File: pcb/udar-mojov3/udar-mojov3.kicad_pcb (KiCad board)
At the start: 2 copper layers, 20 parts, among them J1 Conn_02x03_Odd_Even, M1 Motor_Servo_AirTronics, M2 Motor_Servo_AirTronics, Q1 Q_PNP_BCE, Q2 Q_PNP_BCE, SW1 SW_Push, U1 HC-SR04, U2 ZG-Mxx, U3 Mojov3

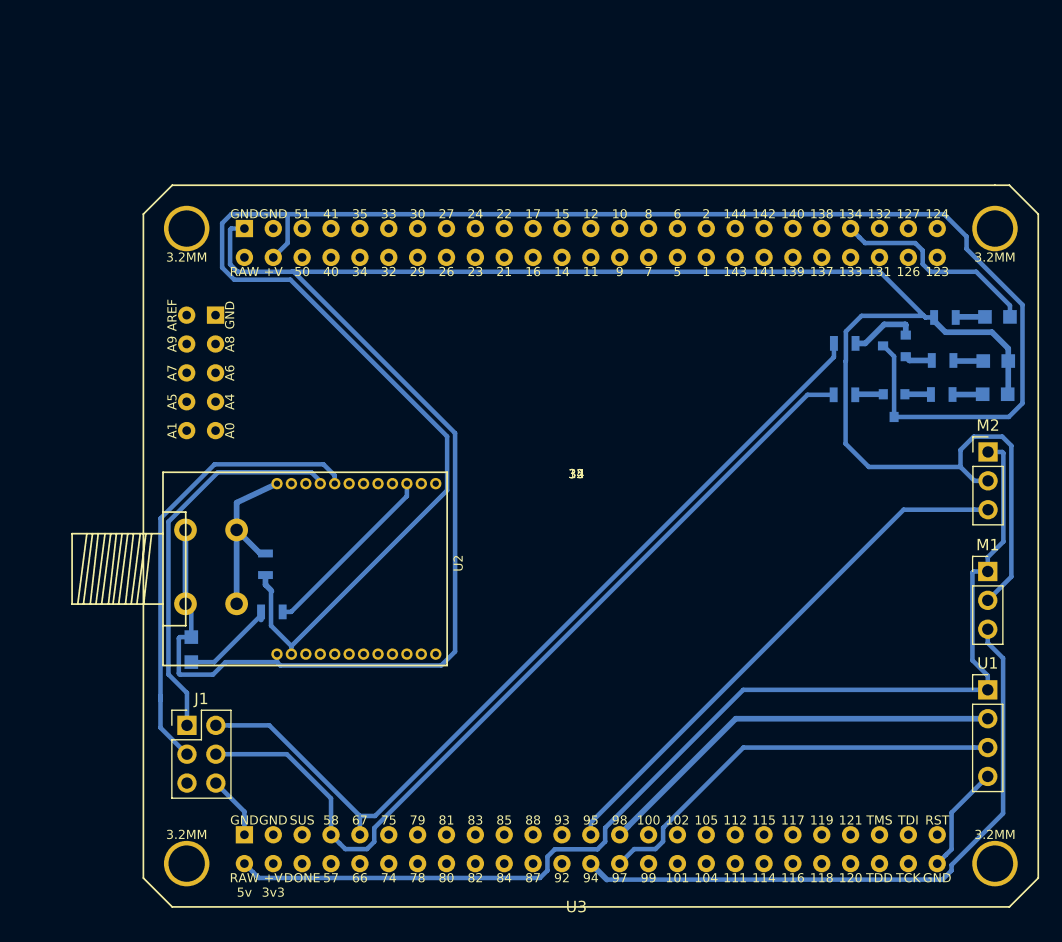
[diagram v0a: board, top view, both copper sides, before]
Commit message: Update
1. Restruct the PCB
2. Change 1602 to OLED(12864)
3. Finish PCB
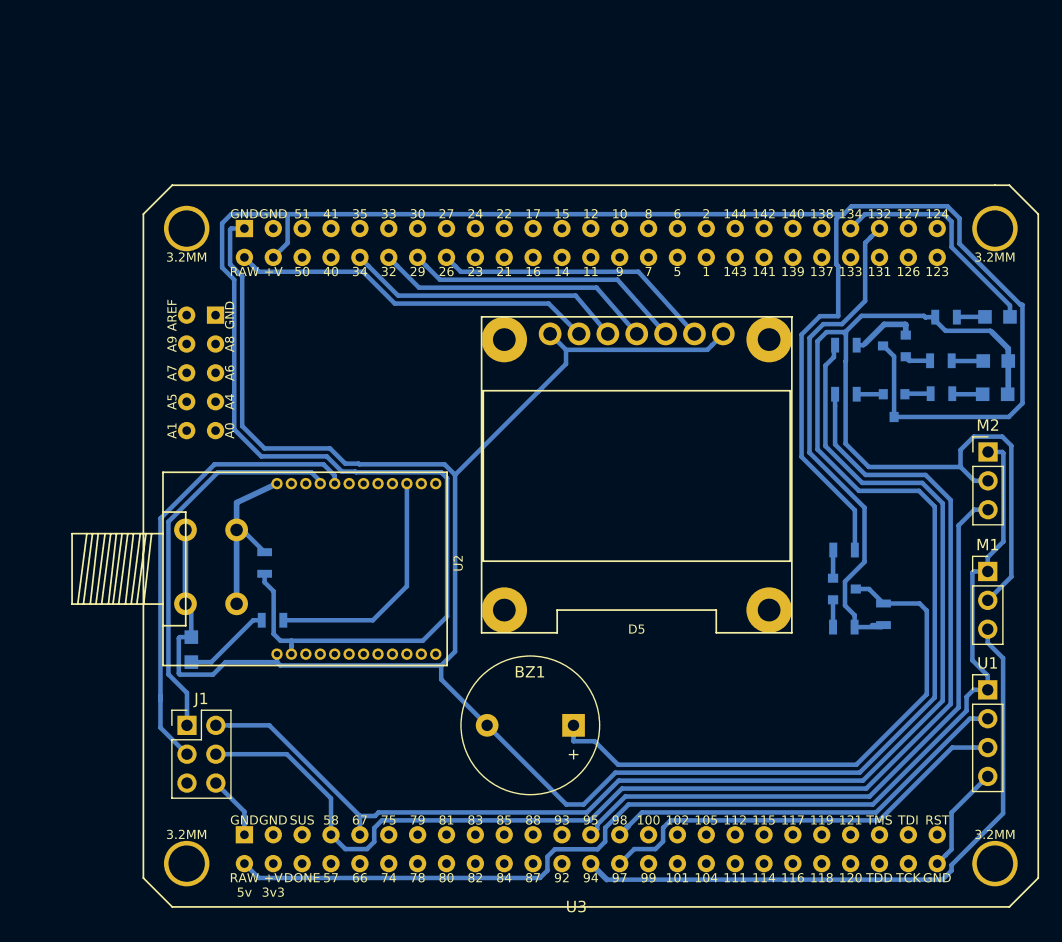
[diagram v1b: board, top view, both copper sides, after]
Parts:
- removed R11: R, Resistors_SMD:R_0805
- added BZ1: Buzzer, Buzzers_Beepers:Buzzer_12x9.5RM7.6, F.Cu at (148.4, 128.6)
- added D5: OLED, OLED:OLED_096_12864_SSD1306, F.Cu at (153.9, 94.2)
- added Q3: Q_NPN_BCE, TO_SOT_Packages_SMD:SOT-23, B.Cu at (172.2, 116.6)
- added R1: R, Resistors_SMD:R_0805, B.Cu at (121.2, 114.3)
- added R2: R, Resistors_SMD:R_0805, B.Cu at (121.9, 119.4)
- added R3: R, Resistors_SMD:R_0805, B.Cu at (172.3, 95.2)
- added R4: R, Resistors_SMD:R_0805, B.Cu at (180.7, 96.5)
- moved R6 62.0 mm to (180.7, 99.4)
- moved R5 53.2 mm to (172.3, 99.5), turned to 180 degrees
- moved R8 25.0 mm to (172.1, 120.0), turned to 180 degrees
- moved R9 19.6 mm to (175.6, 118.9), turned to 90 degrees
- moved R7 18.2 mm to (172.2, 113.2)
- moved R10 6.82 mm to (181.1, 92.7), turned to 180 degrees
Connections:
- net /UDAR-1602a.sch/D0 renamed Net-(U3-Pad33)
- net /UDAR-1602a.sch/D2 renamed Net-(U3-Pad30)
- net /UDAR-1602a.sch/D4 renamed Net-(U3-Pad27)
- net /UDAR-1602a.sch/D6 renamed Net-(U3-Pad24)
- net /UDAR-1602a.sch/D7 renamed Net-(U3-Pad23)
- net /UDAR-1602a.sch/R/W renamed Net-(U3-Pad35)
- net /UDAR-1602a.sch/RS renamed Net-(U3-Pad40)
- R10 pad 1: Net-(Q2-Pad2) -> Net-(D4-Pad1)
- R10 pad 2: Net-(D3-Pad2) -> GND
- R5 pad 1: +3V3 -> Net-(Q2-Pad1)
- R5 pad 2: Net-(R5-Pad2) -> /UART/UART_RX
- R6 pad 1: Net-(D1-Pad2) -> Net-(Q2-Pad2)
- R6 pad 2: Net-(R6-Pad2) -> Net-(D3-Pad2)
- R7 pad 1: Net-(Q1-Pad1) -> +3V3
- R7 pad 2: /UART/UART_TX -> Net-(Q3-Pad2)
- R8 pad 1: Net-(Q1-Pad2) -> Net-(R8-Pad1)
- R8 pad 2: Net-(D2-Pad2) -> Net-(Q3-Pad1)
- R9 pad 1: Net-(Q2-Pad1) -> Net-(R8-Pad1)
- R9 pad 2: /UART/UART_RX -> Net-(BZ1-Pad1)
- SW1 pad 1: Net-(R5-Pad2) -> Net-(R1-Pad2)
- U2 pad B1: Net-(R5-Pad2) -> Net-(R1-Pad2)
- U2 pad B10: Net-(R6-Pad2) -> Net-(R2-Pad2)
- U3 pad 132: Net-(U3-Pad132) -> Net-(R8-Pad1)
- U3 pad 26: /UDAR-1602a.sch/D5 -> /0.96 OLED/DC
- U3 pad 29: /UDAR-1602a.sch/D3 -> /0.96 OLED/RST
- U3 pad 32: /UDAR-1602a.sch/D1 -> /0.96 OLED/DATA
- U3 pad 34: /UDAR-1602a.sch/E -> /0.96 OLED/CLK
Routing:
- net GND: track 227.4 -> 302.3 mm
- net Net-(BZ1-Pad1): track 0.00 -> 50.3 mm
- net +3V3: track 168.2 -> 216.1 mm
- net Net-(R8-Pad1): track 0.00 -> 45.3 mm
- net /UART/UART_TX: track 77.3 -> 112.1 mm
- net /UART/UART_RX: track 77.3 -> 110.6 mm
- net +5V: track 98.8 -> 131.8 mm
- net /0.96 OLED/CLK: track 0.00 -> 24.8 mm
- net /0.96 OLED/DATA: track 0.00 -> 24.8 mm
- net /0.96 OLED/RST: track 0.00 -> 24.8 mm
- net /0.96 OLED/DC: track 0.00 -> 24.8 mm
- net Net-(R2-Pad2): track 0.00 -> 21.7 mm
- net Net-(R1-Pad2): track 0.00 -> 16.6 mm
- net Net-(R6-Pad2): track 16.3 -> 0.00 mm
- net Net-(R5-Pad2): track 16.2 -> 0.00 mm
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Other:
- net class self: clearance 0.3 -> 0.2
- net class self-m added: clearance 0.2, trace_width 0.4, via_dia 0.6, via_drill 0.4

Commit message: Update for 0.1-alpha1
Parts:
- added U4: AP1117-50, TO_SOT_Packages_SMD:SOT-223-3_TabPin2, B.Cu at (127.4, 96.3)
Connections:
- U3 pad RAW: +5V -> Net-(U3-PadRAW)
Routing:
- net +5V: track 131.8 -> 181.4 mm
- net Net-(U3-PadRAW): track 0.00 -> 14.1 mm
- net GND: track 302.3 -> 308.3 mm
- net +3V3: track 216.1 -> 215.5 mm

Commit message: Update;
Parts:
- moved D2 14.9 mm to (181.2, 82.3)
- moved D3 14.9 mm to (181.2, 85.3)
- moved D4 14.9 mm to (181.4, 78.5)
- moved D5 14.9 mm to (149.7, 80.0)
- moved Q1 14.9 mm to (172.3, 81.0)
- moved Q2 14.9 mm to (172.3, 86.3)
- moved Q3 14.9 mm to (167.9, 102.4)
- moved R3 14.9 mm to (168.1, 80.9)
- moved R5 14.9 mm to (168.1, 85.3)
- moved R6 14.9 mm to (176.5, 85.2)
- moved R7 14.9 mm to (167.9, 99.0)
- moved R9 14.9 mm to (171.4, 104.6)
- moved U3 14.9 mm to (144.3, 92.3)
- moved U2 14.9 mm to (119.0, 100.6)
- moved M1 14.9 mm to (180.5, 100.9)
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
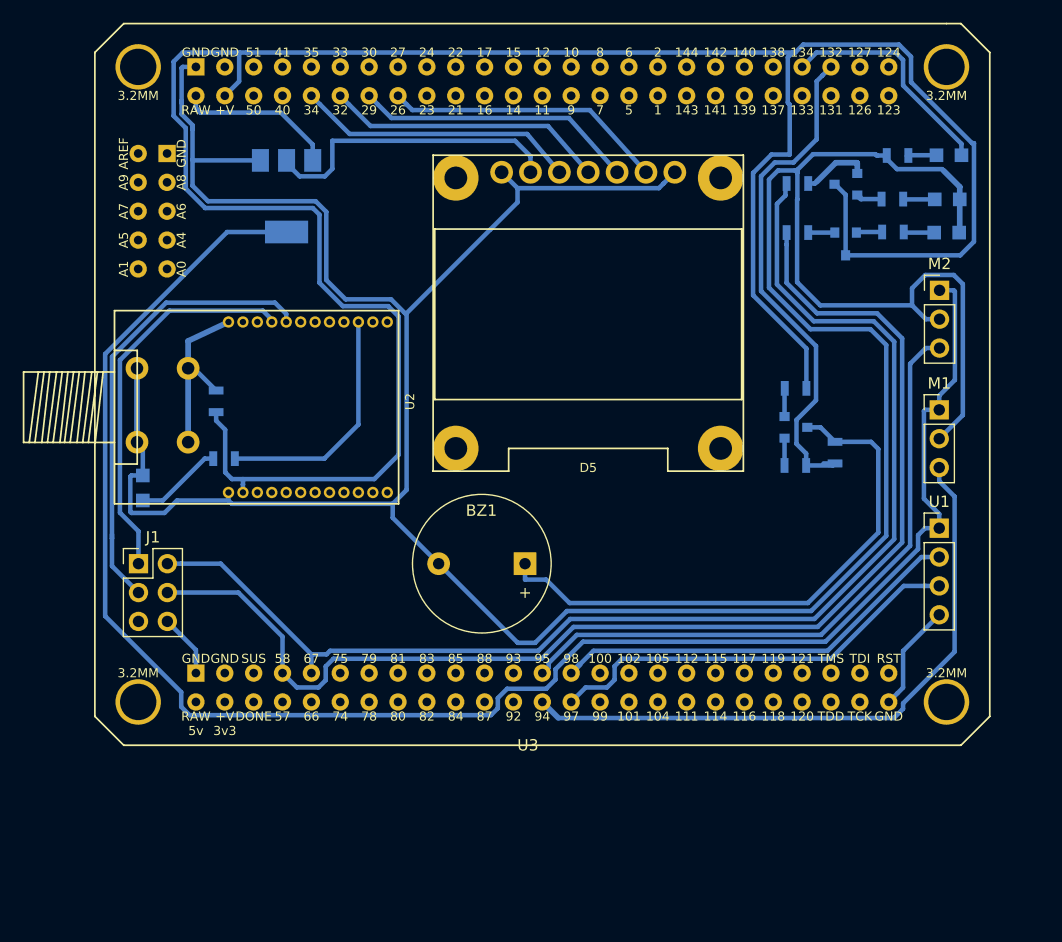
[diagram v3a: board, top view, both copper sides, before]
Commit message: Update (Card-10280892 step 1)
1. Store 1 to 5 are done
   modified:   hardware_description/ctrl.v

2. Store 1 to 5 are verified
   modified:   hardware_description/test_bench/ctrl_tb.v

3. Add the ``.ignore'' into ``.gitignore'' file.
   modified:   .gitignore

4. Update the top module(both top module and I/O pins)
   modified:   hardware_description/.ise_project/src/mojo_top.v
   modified:   hardware_description/.ise_project/src/mojo.ucf

5. Change the UART's rx and tx to P57 and P58(both sch. file and pcb board).
   modified:   pcb/udar-mojov3/udar-mojov3.kicad_pcb
   modified:   pcb/udar-mojov3/UART.sch
   modified:   pcb/udar-mojov3/UDAR-board.sch

*  The IDEs update files automatically.
   modified:   hardware_description/.ise_project/Mojo-Base.xise
   modified:   hardware_description/.ise_project/iseconfig/Mojo-Base.projectmgr
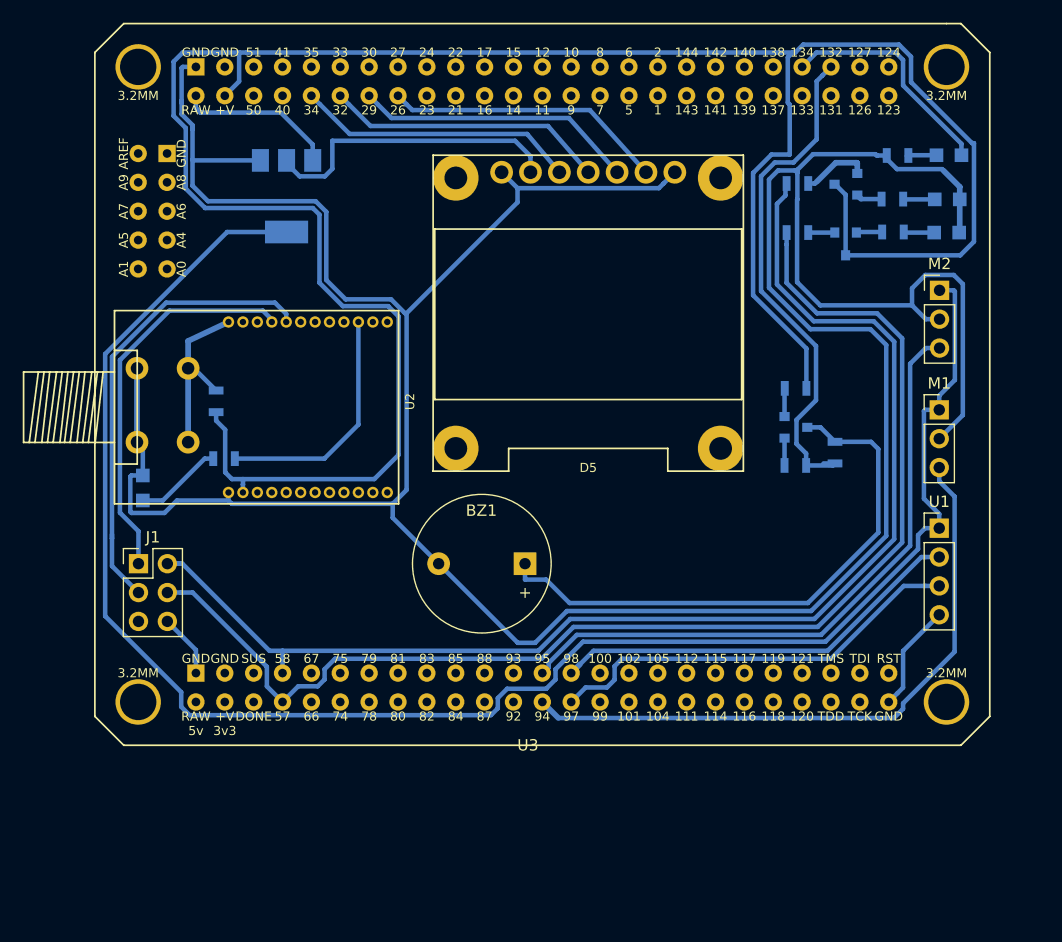
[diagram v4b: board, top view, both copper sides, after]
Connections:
- U3 pad 57: Net-(U3-Pad57) -> /UART/UART_RX
- U3 pad 58: /UART/UART_RX -> /UART/UART_TX
- U3 pad 67: /UART/UART_TX -> Net-(U3-Pad67)
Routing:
- net /UART/UART_TX: track 112.1 -> 113.4 mm
